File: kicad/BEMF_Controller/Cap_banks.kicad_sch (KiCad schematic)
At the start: 63 parts

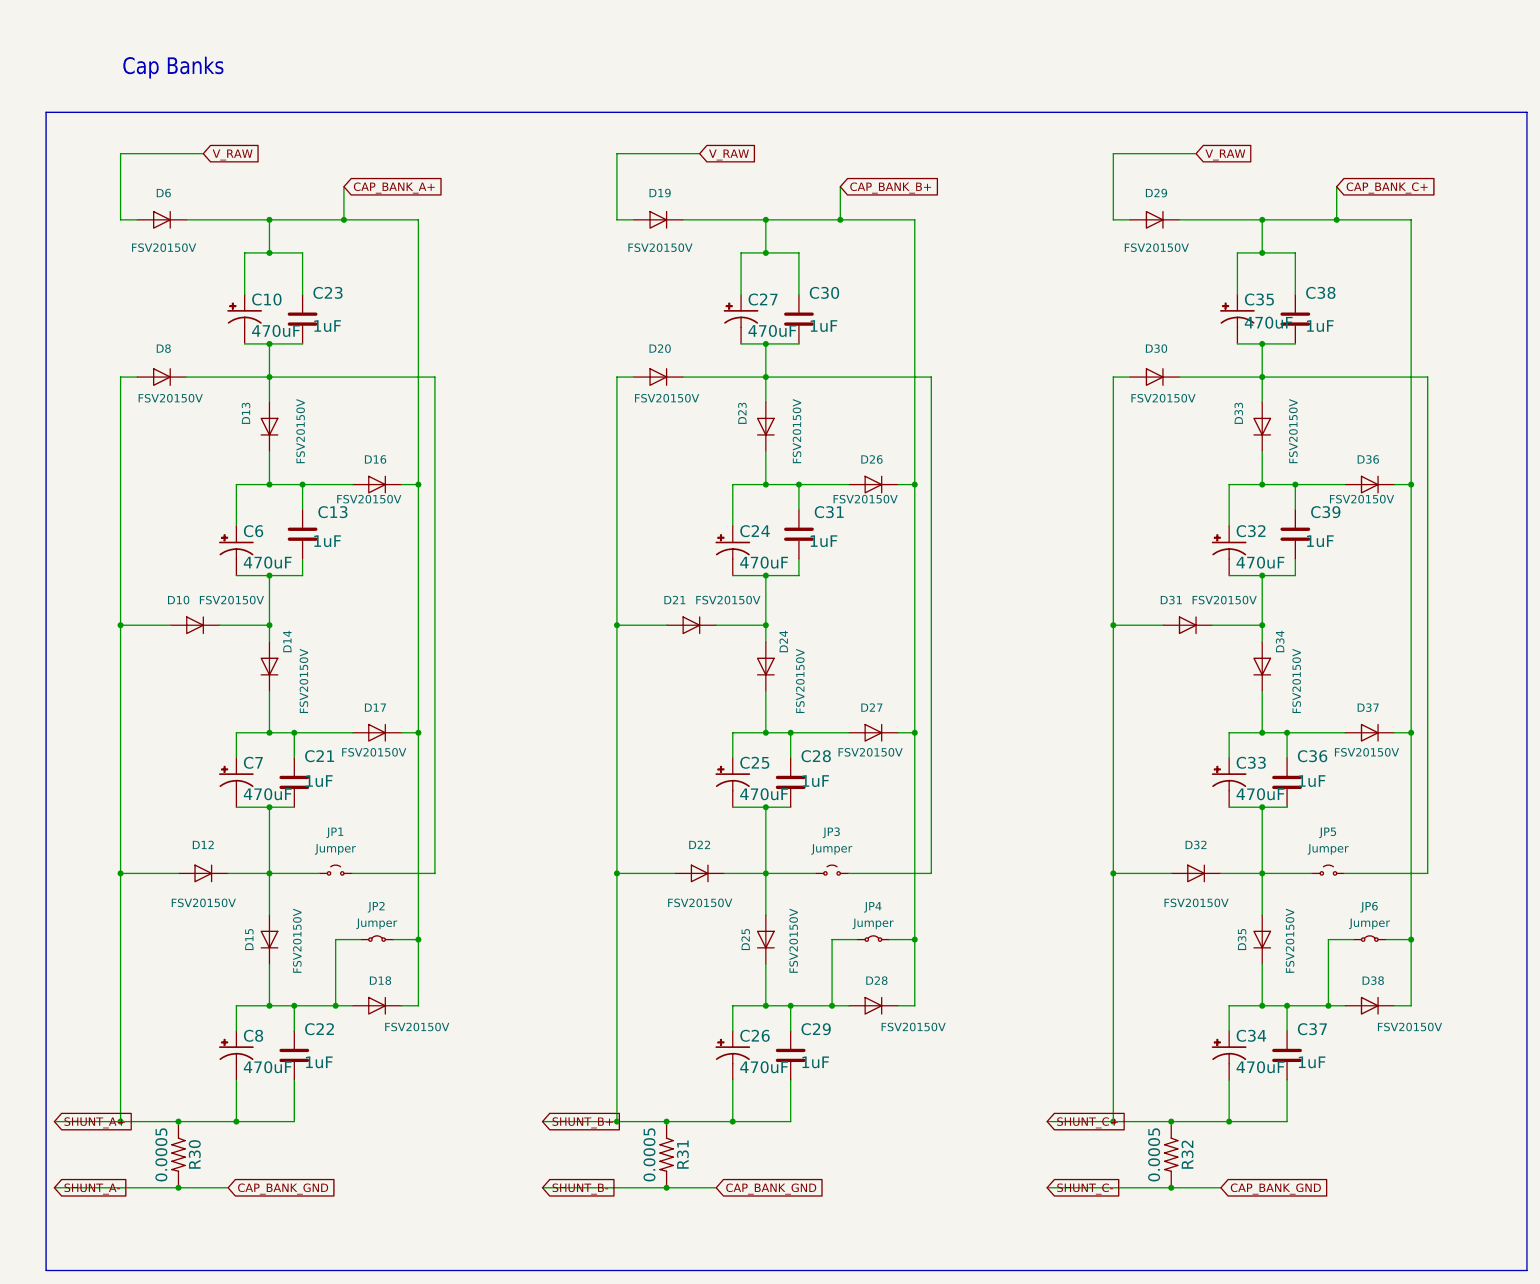
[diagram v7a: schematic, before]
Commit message: Feature complete, zero eroors in pcb. Still lot of warnings.
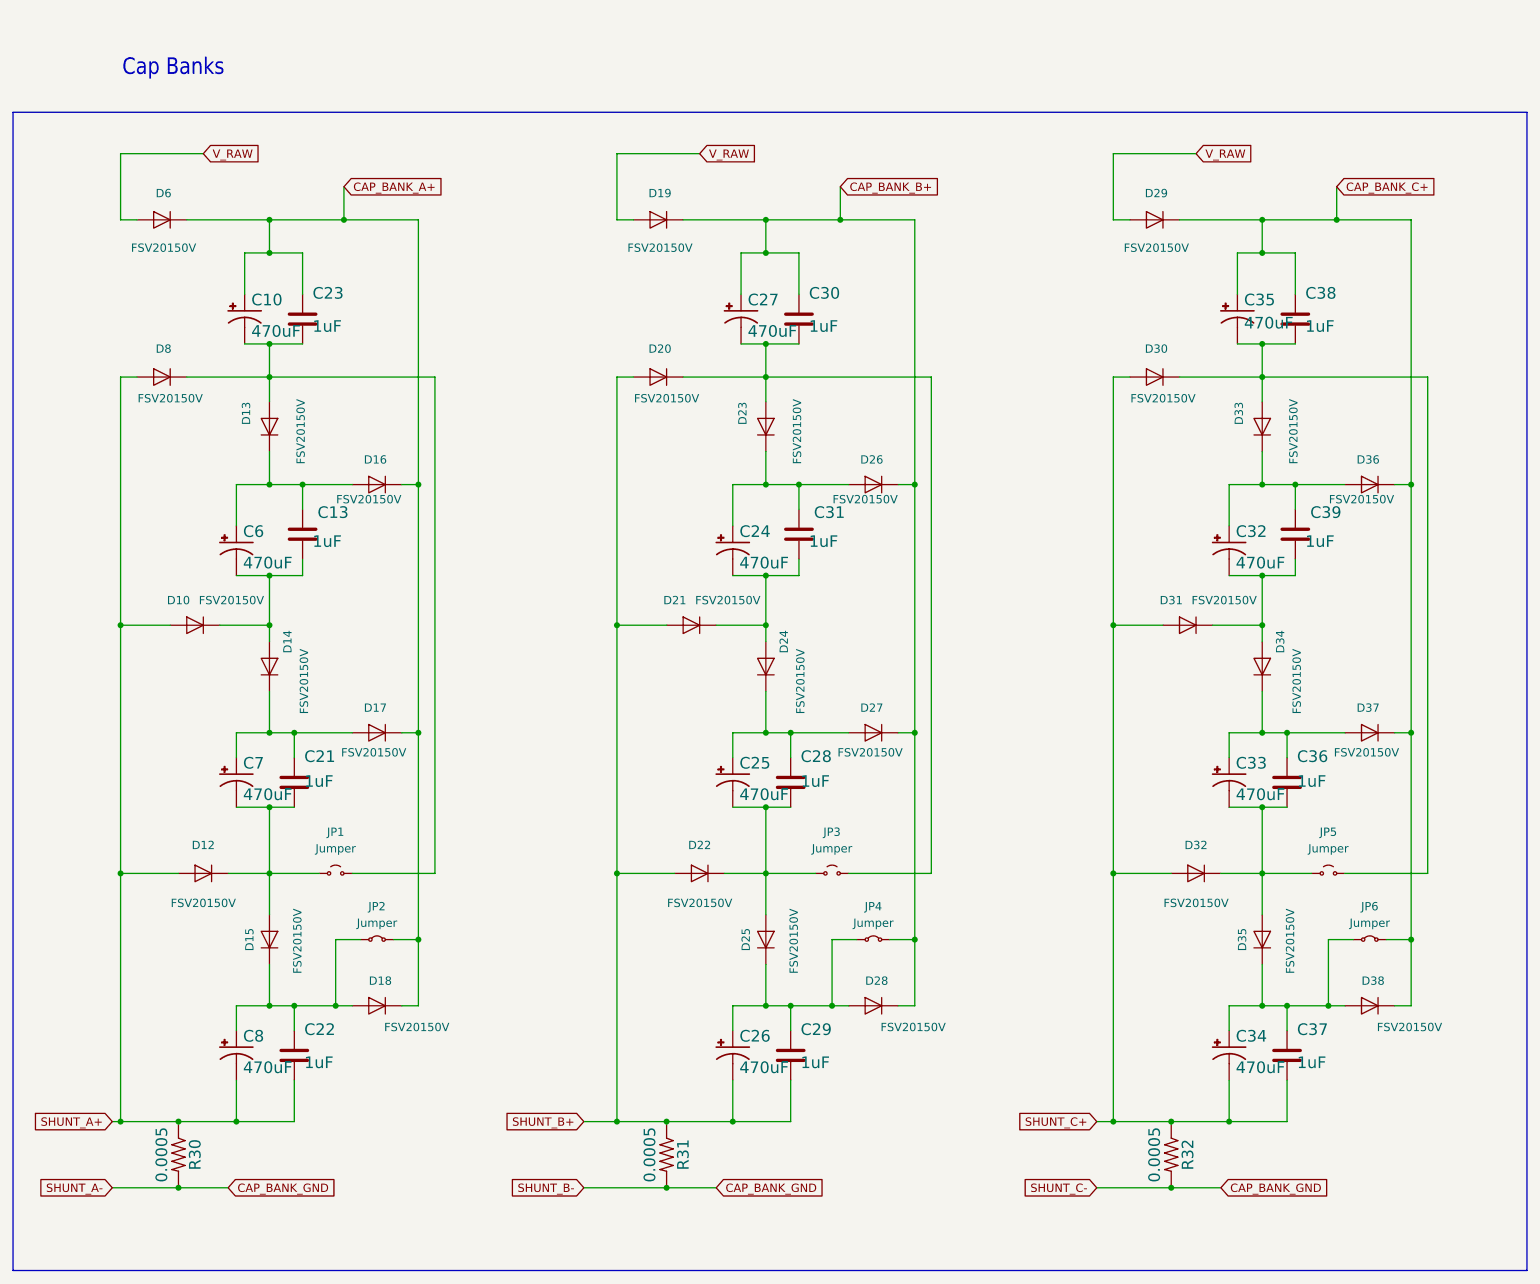
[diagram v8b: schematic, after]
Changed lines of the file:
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@@
+	)
+	(junction
+		(at 97.79 175.26)
+		(diameter 0)
+		(color 0 0 0 0)
 	)
 	(junction
@@
 	)
 	(junction
-		(at 97.79 175.26)
-		(diameter 0)
-		(color 0 0 0 0)
-	)
-	(junction
 		(at 196.85 99.06)
 		(diameter 0)
@@
 	(wire
 		(pts
-			(xy 11.43 175.26) (xy 21.59 175.26)
-		)
-		(stroke
-			(width 0)
-			(type default)
-		)
-	)
-	(wire
-		(pts
 			(xy 193.04 41.91) (xy 196.85 41.91)
 		)
@@
 	(wire
 		(pts
-			(xy 86.36 175.26) (xy 97.79 175.26)
+			(xy 92.71 175.26) (xy 97.79 175.26)
 		)
 		(stroke
@@
 	(wire
 		(pts
-			(xy 182.88 185.42) (xy 163.83 185.42)
+			(xy 182.88 185.42) (xy 171.45 185.42)
 		)
 		(stroke
@@
 	(wire
 		(pts
-			(xy 30.48 185.42) (xy 11.43 185.42)
+			(xy 30.48 185.42) (xy 20.32 185.42)
 		)
 		(stroke
@@
 	(wire
 		(pts
+			(xy 92.71 185.42) (xy 105.41 185.42)
+		)
+		(stroke
+			(width 0)
+			(type default)
+		)
+	)
+	(wire
+		(pts
 			(xy 44.45 151.13) (xy 44.45 157.48)
 		)
@@
 	(wire
 		(pts
-			(xy 163.83 175.26) (xy 173.99 175.26)
+			(xy 171.45 175.26) (xy 173.99 175.26)
 		)
 		(stroke
@@
 	(wire
 		(pts
-			(xy 105.41 185.42) (xy 86.36 185.42)
-		)
-		(stroke
-			(width 0)
-			(type default)
-		)
-	)
-	(wire
-		(pts
 			(xy 120.65 99.06) (xy 120.65 101.6)
 		)
@@
 	(wire
 		(pts
+			(xy 20.32 175.26) (xy 21.59 175.26)
+		)
+		(stroke
+			(width 0)
+			(type default)
+		)
+	)
+	(wire
+		(pts
 			(xy 222.25 137.16) (xy 222.25 60.96)
 		)
@@
 	)
 	(rectangle
-		(start 10.16 20.32)
+		(start 5.08 20.32)
 		(end 237.49 198.12)
 		(stroke
@@
 	(global_label "SHUNT_A-"
 		(shape input)
-		(at 11.43 185.42 0)
+		(at 20.32 185.42 180)
 		(fields_autoplaced yes)
 		(effects
@@
 				(size 1.27 1.27)
 			)
-			(justify left)
+			(justify right)
 		)
 		(property "Intersheetrefs" "${INTERSHEET_REFS}"
-			(at 24.2124 185.42 0)
+			(at 7.5376 185.42 0)
 			(effects
 				(font
 					(size 1.27 1.27)
 				)
-				(justify left)
+				(justify right)
 				(hide yes)
 			)
@@
 	(global_label "SHUNT_B+"
 		(shape input)
-		(at 86.36 175.26 0)
+		(at 92.71 175.26 180)
 		(fields_autoplaced yes)
 		(effects
@@
 				(size 1.27 1.27)
 			)
-			(justify left)
+			(justify right)
 		)
 		(property "Intersheetrefs" "${INTERSHEET_REFS}"
-			(at 99.3238 175.26 0)
+			(at 79.7462 175.26 0)
 			(effects
 				(font
 					(size 1.27 1.27)
 				)
-				(justify left)
+				(justify right)
 				(hide yes)
 			)
@@
 	(global_label "SHUNT_C-"
 		(shape input)
-		(at 163.83 185.42 0)
+		(at 171.45 185.42 180)
 		(fields_autoplaced yes)
 		(effects
@@
 				(size 1.27 1.27)
 			)
-			(justify left)
+			(justify right)
 		)
 		(property "Intersheetrefs" "${INTERSHEET_REFS}"
-			(at 176.7938 185.42 0)
+			(at 158.4862 185.42 0)
 			(effects
 				(font
 					(size 1.27 1.27)
 				)
-				(justify left)
+				(justify right)
 				(hide yes)
 			)
@@
 	(global_label "SHUNT_B-"
 		(shape input)
-		(at 86.36 185.42 0)
+		(at 92.71 185.42 180)
 		(fields_autoplaced yes)
 		(effects
@@
 				(size 1.27 1.27)
 			)
-			(justify left)
+			(justify right)
 		)
 		(property "Intersheetrefs" "${INTERSHEET_REFS}"
-			(at 99.3238 185.42 0)
+			(at 79.7462 185.42 0)
 			(effects
 				(font
 					(size 1.27 1.27)
 				)
-				(justify left)
+				(justify right)
 				(hide yes)
 			)
@@
 	(global_label "SHUNT_C+"
 		(shape input)
-		(at 163.83 175.26 0)
+		(at 171.45 175.26 180)
 		(fields_autoplaced yes)
 		(effects
@@
 				(size 1.27 1.27)
 			)
-			(justify left)
+			(justify right)
 		)
 		(property "Intersheetrefs" "${INTERSHEET_REFS}"
-			(at 176.7938 175.26 0)
+			(at 158.4862 175.26 0)
 			(effects
 				(font
 					(size 1.27 1.27)
 				)
-				(justify left)
+				(justify right)
 				(hide yes)
 			)
@@
 	(global_label "SHUNT_A+"
 		(shape input)
-		(at 11.43 175.26 0)
+		(at 20.32 175.26 180)
 		(fields_autoplaced yes)
 		(effects
@@
 				(size 1.27 1.27)
 			)
-			(justify left)
+			(justify right)
 		)
 		(property "Intersheetrefs" "${INTERSHEET_REFS}"
-			(at 24.2124 175.26 0)
+			(at 7.5376 175.26 0)
 			(effects
 				(font
 					(size 1.27 1.27)
 				)
-				(justify left)
+				(justify right)
 				(hide yes)
 			)
